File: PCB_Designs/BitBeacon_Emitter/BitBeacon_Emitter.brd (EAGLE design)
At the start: 100 x 80 mm, 9 parts, among them IC1 AD8607RM, IC2 AD8603UJ, Q1 TIP120

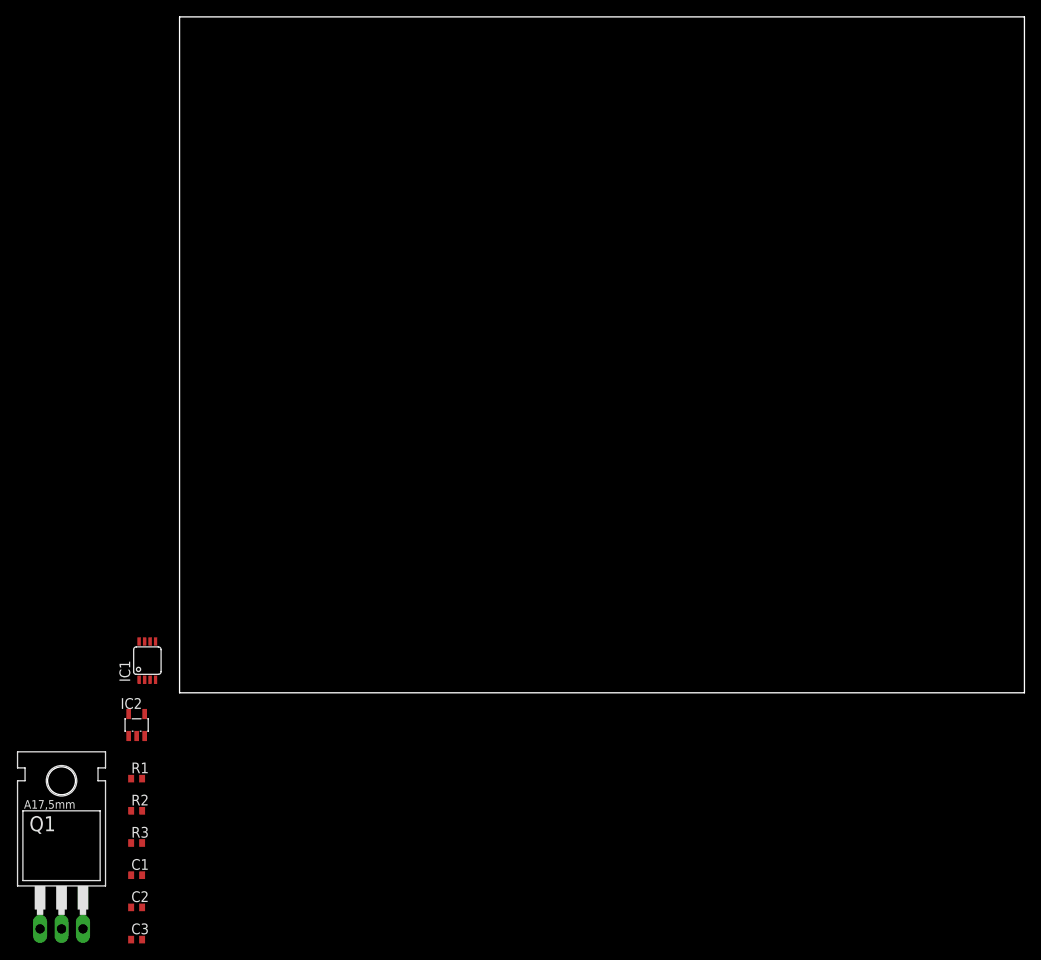
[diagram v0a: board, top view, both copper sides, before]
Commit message: updating pcb files for emitter circuit
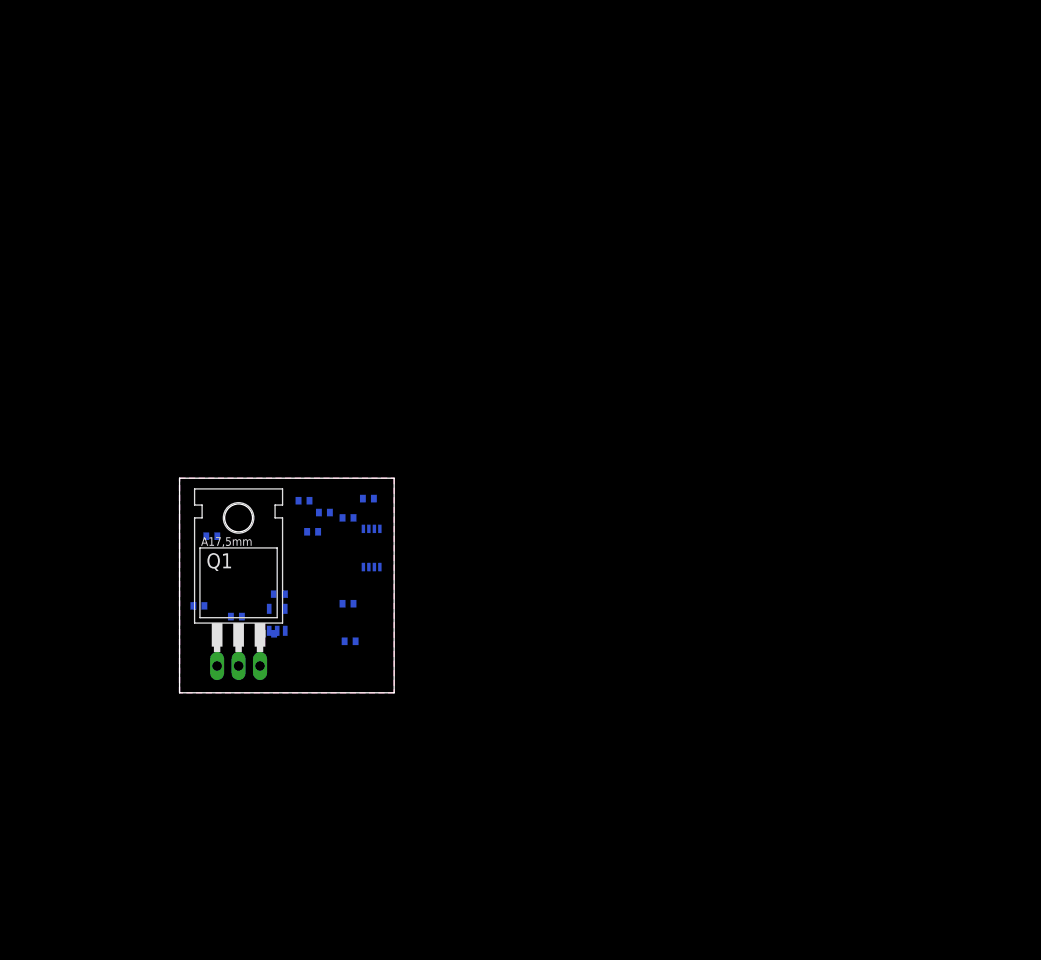
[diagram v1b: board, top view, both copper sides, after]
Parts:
- added C4, C5, C6: 100n, resistor:C0402
- added R4: 2k, resistor:R0402
- added R5: 10k, resistor:R0402
- added R6: (no value), resistor:R0402
- moved C3 55.8 mm to (19.9, 20.7), flipped to the bottom
- moved C2 40.4 mm to (20.2, 6.10), flipped to the bottom
- moved R1 38.5 mm to (17.1, 21.3), flipped to the bottom
- moved Q1 37.5 mm to (6.99, 9.53)
- moved C1 37.3 mm to (11.8, 11.7), flipped to the bottom
- moved R2 35.0 mm to (19.9, 10.5), flipped to the bottom
- moved IC1 29.7 mm to (22.7, 17.1), flipped to the bottom
- moved R3 29.3 mm to (6.73, 9.02), flipped to the bottom
- moved IC2 20.8 mm to (11.6, 8.64), flipped to the bottom
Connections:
- removed net V+: IC1.8
- removed net V-: IC1.4
- new net 5V: C4.2, C5.1, C6.1, IC1.8, IC2.5, Q1.C, R4.2
- new net GND: C3.1, C4.1, C5.2, C6.2, IC1.4, IC2.2, R5.2
- new net N$12: Q1.B, R6.1
- new net N$3: C1.1, IC1.2, R2.2
- new net N$6: IC1.3, IC2.1, IC2.4, R1.1
- new net N$7: IC2.3, R4.1, R5.1
- net N$1: now also C1.2, R6.2
- net N$4: now also R2.1
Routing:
- added copper zone on layer 1, net GND
- added copper zone on layer 16, net GND
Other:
- board size 100 x 80 mm -> 25.4 x 25.4 mm

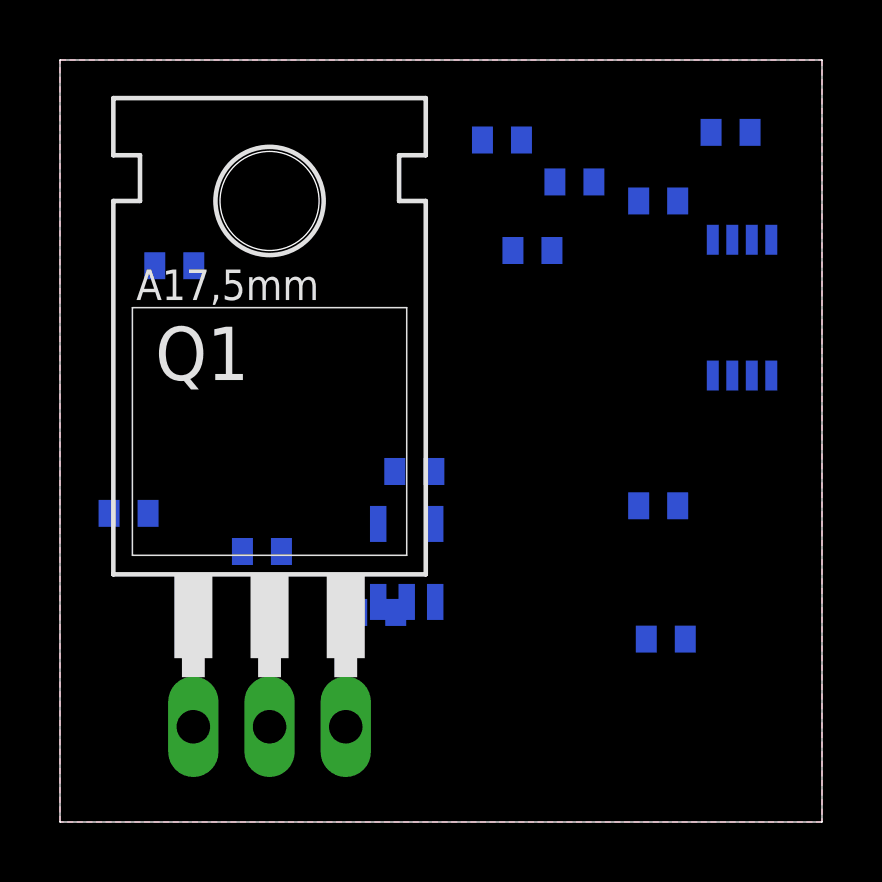
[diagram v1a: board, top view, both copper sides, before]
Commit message: finished PCB design for Bit Beacon Emitter circuit and added datsheets for the LEDs that I think would work well.
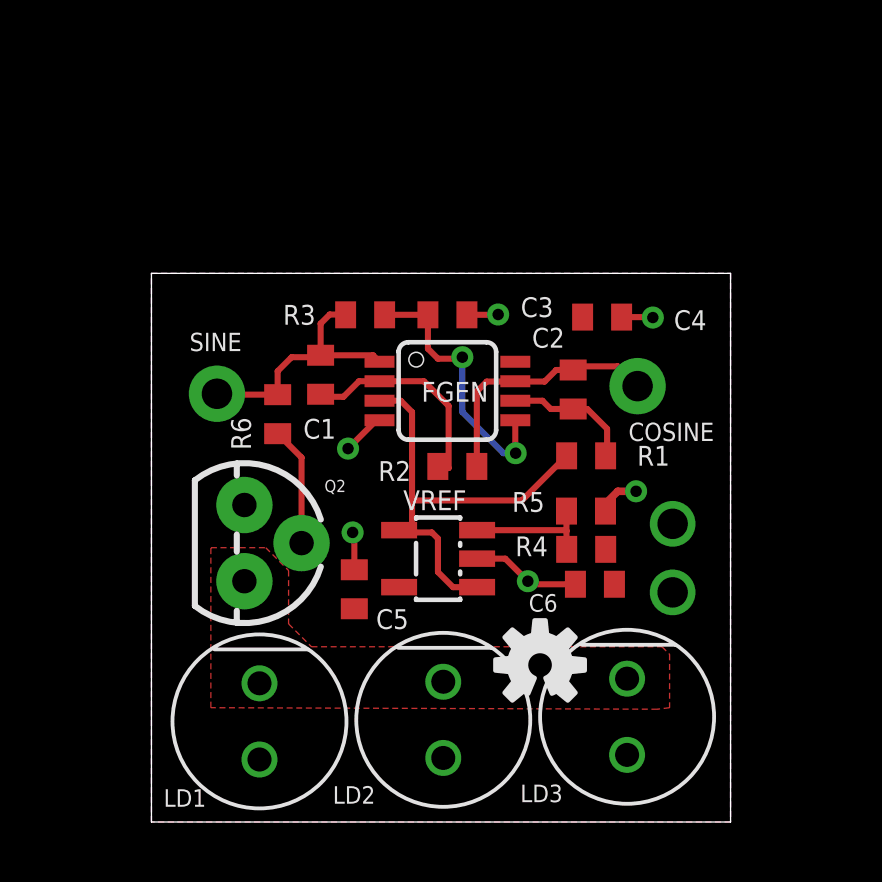
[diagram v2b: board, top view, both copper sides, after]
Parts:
- removed IC1: AD8607RM, analog-devices:MSOP08
- removed IC2: AD8603UJ, analog-devices:SOT23-5
- removed Q1: TIP120, transistor-power:TO220AH
- added FGEN: (no value), analog-devices:MSOP08
- added JP1, JP2: M01NOSILK-KIT, SparkFun-Connectors:1X01NS-KIT
- added LED1, LED2, LED3: LED, Orlando:LED
- added LOGO1: OSHW-LOGOS, SparkFun-Aesthetics:OSHW-LOGO-S
- added Q2: (no value), SparkFun-DiscreteSemi:TO-92
- added U$1: BATT-CONNECT, OrlandoRonMod:HOLE
- added VREF: (no value), analog-devices:SOT23-5
- C6: value 100n -> (none)
- R4: value 2k -> 5.1k
- moved C5 19.7 mm to (9.81, 7.76), flipped to the top, turned to 90 degrees
- moved C4 14.4 mm to (18.1, 16.8), flipped to the top, turned to 180 degrees
- moved R5 12.7 mm to (17.5, 10.4), flipped to the top
- moved R4 10.1 mm to (17.5, 9.09), flipped to the top
- moved R1 9.14 mm to (17.5, 12.2), flipped to the top
- moved C2 8.88 mm to (17.1, 14.4), flipped to the top, turned to 270 degrees
- moved R3 8.61 mm to (10.2, 16.9), flipped to the top, turned to 180 degrees
- moved C3 7.98 mm to (12.9, 16.9), flipped to the top, turned to 180 degrees
- moved C6 7.35 mm to (17.8, 7.92), flipped to the top, turned to 180 degrees
- moved R2 6.82 mm to (13.2, 11.9), flipped to the top, turned to 180 degrees
- moved R6 5.97 mm to (7.25, 13.6), flipped to the top, turned to 90 degrees
- moved C1 4.49 mm to (8.69, 14.9), flipped to the top, turned to 90 degrees
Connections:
- removed net N$1: C1.2, IC1.1, R3.2, R6.2
- removed net N$12: Q1.B, R6.1
- removed net N$4: C2.1, IC1.7, R2.1
- new net COSINE: C2.1, FGEN.7, JP2.1, R2.1
- new net N$8: LED1.C, LED2.C, LED3.C, Q2.3
- new net N$9: Q2.2, R6.1
- new net SINE: C1.2, FGEN.1, JP1.1, R3.2, R6.2
- net 5V: now also FGEN.8, LED1.A, LED2.A, LED3.A, U$1.P$2, VREF.5; no longer IC1.8, IC2.5, Q1.C
- net GND: now also FGEN.4, Q2.1, U$1.P$1, VREF.2; no longer IC1.4, IC2.2
- net N$2: now also FGEN.5; no longer IC1.5
- net N$3: now also FGEN.2; no longer IC1.2
- net N$5: now also FGEN.6; no longer IC1.6
- net N$6: now also FGEN.3, VREF.1, VREF.4; no longer IC1.3, IC2.1, IC2.4
- net N$7: now also VREF.3; no longer IC2.3
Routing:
- net N$6: track 0.00 -> 15.1 mm
- net GND: track 0.00 -> 9.86 mm, vias 0 -> 6
- net N$2: track 0.00 -> 9.16 mm, vias 0 -> 2
- net SINE: track 0.00 -> 8.54 mm
- net COSINE: track 0.00 -> 8.49 mm
- net N$3: track 0.00 -> 7.29 mm
- net N$5: track 0.00 -> 4.37 mm
- net N$7: track 0.00 -> 4.27 mm
- net N$9: track 0.00 -> 3.98 mm
- added copper zone on layer 1, net 5V
- added copper zone on layer 1, net N$8
- removed copper zone on layer 1, net GND
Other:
- board size 25.4 x 25.4 mm -> 19.3 x 18.3 mm
- board text added: "Battery"
- board text added: "COSINE"
- board text added: "LD1"
- board text added: "LD2"
- board text added: "LD3"
- board text added: "Orlando S. Hoilett BIT Beacon Sig V.1.0 Calvary Eng, IICEPD"
- board text added: "SINE"

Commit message: updated Bit emitter PCB design with resistor and capacitor values. Added a bill of materials for BitBeacon and BitBeacon_Emitter
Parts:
- C1, C2, C3: value (none) -> 1n
- C6: value (none) -> 100n
- R1, R2, R3: value (none) -> 22k
- R4: value 5.1k -> 22k
- R5: value 10k -> 22k
- R6: value (none) -> 100-400
- renumbered U$1 to BATTERY
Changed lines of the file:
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@@
 <?xml version="1.0" encoding="utf-8"?>
 <!DOCTYPE eagle SYSTEM "eagle.dtd">
-<eagle version="7.4.0">
+<eagle version="7.3.0">
 <drawing>
 <settings>
@@
 <attribute name="VALUE" x="16.033" y="6.8728" size="1.27" layer="27" rot="R90"/>
 </element>
-<element name="R1" library="resistor" package="R0402" value="" x="17.537" y="12.2072" smashed="yes">
+<element name="R1" library="resistor" package="R0402" value="22k" x="17.537" y="12.2072" smashed="yes">
 <attribute name="NAME" x="19.2388" y="11.877" size="0.6604" layer="25"/>
 <attribute name="VALUE" x="16.902" y="10.3022" size="1.27" layer="27"/>
 </element>
-<element name="R2" library="resistor" package="R0402" value="" x="13.2444" y="11.8516" smashed="yes" rot="R180">
+<element name="R2" library="resistor" package="R0402" value="22k" x="13.2444" y="11.8516" smashed="yes" rot="R180">
 <attribute name="NAME" x="11.695" y="12.0294" size="0.6604" layer="25" rot="R180"/>
 <attribute name="VALUE" x="13.8794" y="13.7566" size="1.27" layer="27" rot="R180"/>
 </element>
-<element name="R3" library="resistor" package="R0402" value="" x="10.171" y="16.9062" smashed="yes" rot="R180">
+<element name="R3" library="resistor" package="R0402" value="22k" x="10.171" y="16.9062" smashed="yes" rot="R180">
 <attribute name="NAME" x="8.52" y="17.2364" size="0.6604" layer="25" rot="R180"/>
 <attribute name="VALUE" x="10.806" y="18.8112" size="1.27" layer="27" rot="R180"/>
 </element>
-<element name="C1" library="resistor" package="C0402" value="" x="8.6868" y="14.9074" smashed="yes" rot="R90">
+<element name="C1" library="resistor" package="C0402" value="1n" x="8.6868" y="14.9074" smashed="yes" rot="R90">
 <attribute name="NAME" x="9.1972" y="13.4366" size="0.6604" layer="25" rot="R180"/>
 <attribute name="VALUE" x="10.5918" y="14.2724" size="1.27" layer="27" rot="R90"/>
 </element>
-<element name="C2" library="resistor" package="C0402" value="" x="17.1052" y="14.417" smashed="yes" rot="R270">
+<element name="C2" library="resistor" package="C0402" value="1n" x="17.1052" y="14.417" smashed="yes" rot="R270">
 <attribute name="NAME" x="15.7328" y="15.8098" size="0.6604" layer="25"/>
 <attribute name="VALUE" x="15.2002" y="15.052" size="1.27" layer="27" rot="R270"/>
 </element>
-<element name="C3" library="resistor" package="C0402" value="" x="12.9142" y="16.9062" smashed="yes" rot="R180">
+<element name="C3" library="resistor" package="C0402" value="1n" x="12.9142" y="16.9062" smashed="yes" rot="R180">
 <attribute name="NAME" x="16.4448" y="17.4904" size="0.6604" layer="25" rot="R180"/>
 <attribute name="VALUE" x="13.5492" y="18.8112" size="1.27" layer="27" rot="R180"/>
 </element>
-<element name="R4" library="resistor" package="R0402" value="5.1k" x="17.5392" y="9.088" smashed="yes">
+<element name="R4" library="resistor" package="R0402" value="22k" x="17.5392" y="9.088" smashed="yes">
 <attribute name="NAME" x="15.177" y="8.8594" size="0.6604" layer="25"/>
 <attribute name="VALUE" x="18.2758" y="7.5386" size="0.6604" layer="27"/>
 </element>
-<element name="R5" library="resistor" package="R0402" value="10k" x="17.5332" y="10.3638" smashed="yes">
+<element name="R5" library="resistor" package="R0402" value="22k" x="17.5332" y="10.3638" smashed="yes">
 <attribute name="NAME" x="15.0694" y="10.3384" size="0.6604" layer="25"/>
 <attribute name="VALUE" x="16.8982" y="8.4588" size="1.27" layer="27"/>
@@
 <attribute name="VALUE" x="11.7164" y="7.1234" size="0.6604" layer="27" rot="R90"/>
 </element>
-<element name="R6" library="resistor" package="R0402" value="" x="7.255" y="13.5952" smashed="yes" rot="R90">
+<element name="R6" library="resistor" package="R0402" value="100-400" x="7.255" y="13.5952" smashed="yes" rot="R90">
 <attribute name="NAME" x="6.366" y="12.4014" size="0.6604" layer="25" rot="R90"/>
 <attribute name="VALUE" x="9.16" y="12.9602" size="1.27" layer="27" rot="R90"/>
@@
 <element name="JP2" library="SparkFun-Connectors" package="1X01NS-KIT" value="M01NOSILK-KIT" x="19.2532" y="14.5288" smashed="yes"/>
 <element name="LOGO1" library="SparkFun-Aesthetics" package="OSHW-LOGO-S" value="OSHW-LOGOS" x="16.002" y="5.2324" smashed="yes"/>
-<element name="U$1" library="OrlandoRonMod" package="HOLE" value="BATT-CONNECT" x="20.4216" y="8.7884" rot="R270"/>
-<element name="C6" library="resistor" package="C0402" value="" x="17.8308" y="7.9248" smashed="yes" rot="R180">
+<element name="BATTERY" library="OrlandoRonMod" package="HOLE" value="BATT-CONNECT" x="20.4216" y="8.7884" rot="R270"/>
+<element name="C6" library="resistor" package="C0402" value="100n" x="17.8308" y="7.9248" smashed="yes" rot="R180">
 <attribute name="NAME" x="16.5862" y="7.5946" size="0.5842" layer="25" rot="R180"/>
 <attribute name="VALUE" x="18.4658" y="9.8298" size="1.27" layer="27" rot="R180"/>
@@
 <wire x1="19.6952" y1="16.83" x2="19.7612" y2="16.8148" width="0.2032" layer="1"/>
 <via x="19.2024" y="11.0236" extent="1-16" drill="0.381" shape="octagon"/>
-<contactref element="U$1" pad="P$1"/>
+<contactref element="BATTERY" pad="P$1"/>
 <wire x1="18.1832" y1="10.3638" x2="18.1832" y2="10.614" width="0.254" layer="1"/>
 <wire x1="18.1832" y1="10.614" x2="18.5928" y2="11.0236" width="0.254" layer="1"/>
@@
 <contactref element="LED3" pad="A"/>
 <contactref element="LED1" pad="A"/>
-<contactref element="U$1" pad="P$2"/>
+<contactref element="BATTERY" pad="P$2"/>
 <contactref element="C6" pad="1"/>
 </signal>

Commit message: updates to beacon emitter design
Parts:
- R6: value 100-400 -> 10k-50k
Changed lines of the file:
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@@
 <?xml version="1.0" encoding="utf-8"?>
 <!DOCTYPE eagle SYSTEM "eagle.dtd">
-<eagle version="7.3.0">
+<eagle version="7.4.0">
 <drawing>
 <settings>
@@
 <attribute name="VALUE" x="11.7164" y="7.1234" size="0.6604" layer="27" rot="R90"/>
 </element>
-<element name="R6" library="resistor" package="R0402" value="100-400" x="7.255" y="13.5952" smashed="yes" rot="R90">
+<element name="R6" library="resistor" package="R0402" value="10k-50k" x="7.255" y="13.5952" smashed="yes" rot="R90">
 <attribute name="NAME" x="6.366" y="12.4014" size="0.6604" layer="25" rot="R90"/>
 <attribute name="VALUE" x="9.16" y="12.9602" size="1.27" layer="27" rot="R90"/>
